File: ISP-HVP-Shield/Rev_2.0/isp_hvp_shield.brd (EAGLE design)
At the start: 50 x 53 mm, 26 parts, among them IC1 ATtiny13/15/25/45/85, IC2 ATtiny24/44/84, IC3 TINY26/261/461/861, IC4 ATtiny2313/4313, IC5 ATMEGA328, IC6 74HCT595D, IC7 MAX662A, Q1 BC858BSMD

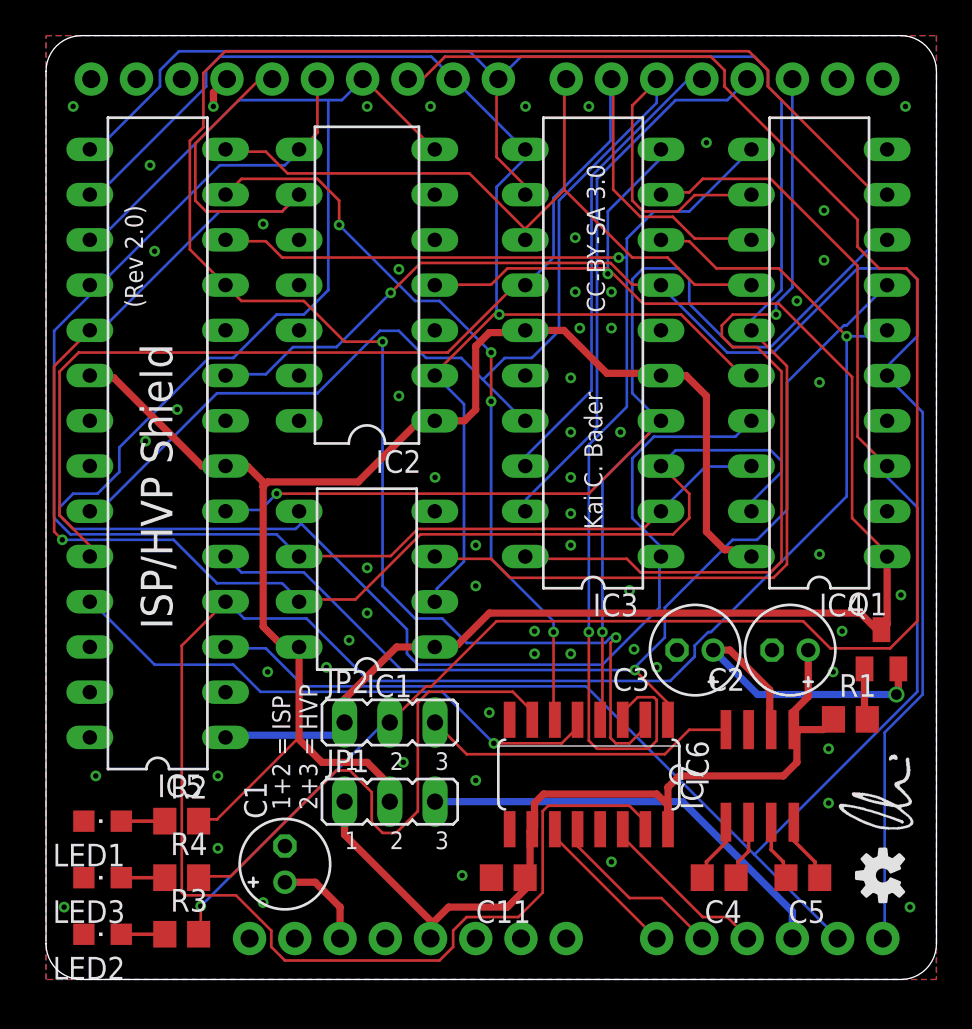
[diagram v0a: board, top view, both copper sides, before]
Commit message: New design. Started to add HVSP/HVPP features.
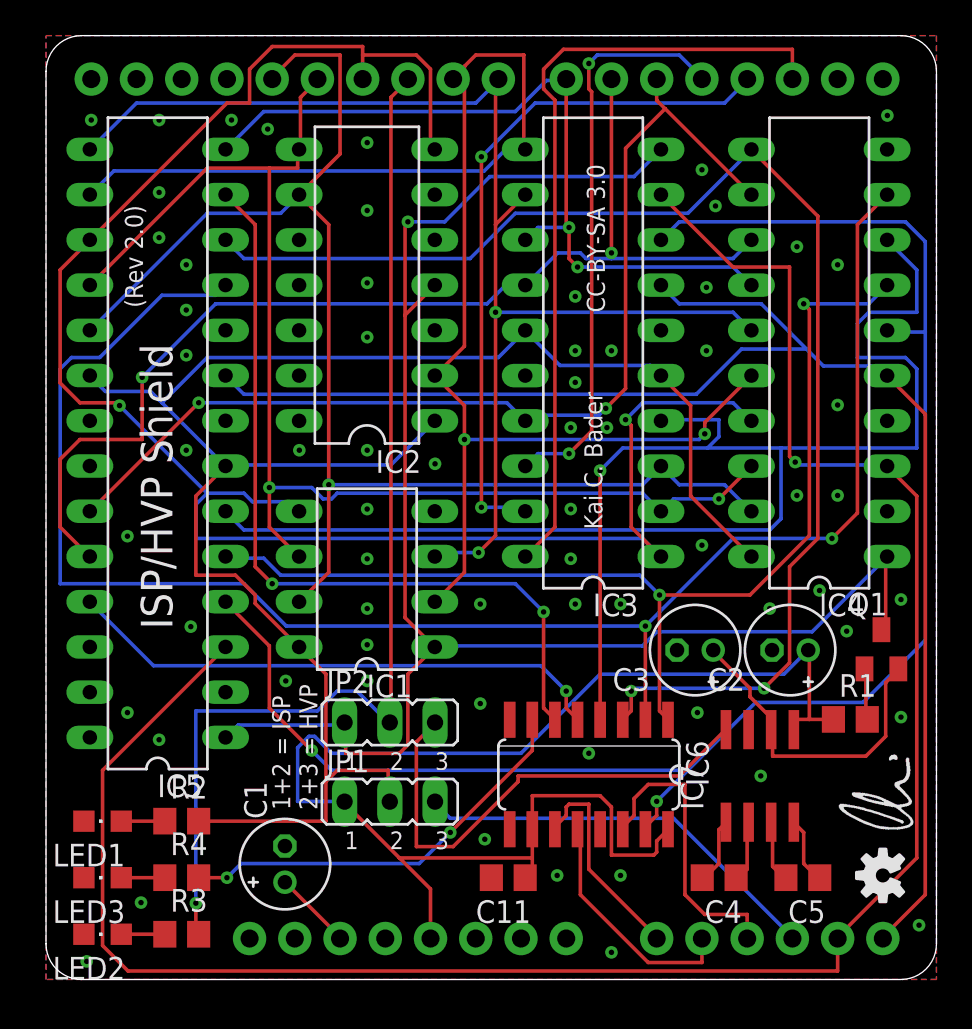
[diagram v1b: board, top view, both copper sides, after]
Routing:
- net D10: track 104.7 -> 61.3 mm
- net D8: track 99.7 -> 71.4 mm, vias 0 -> 2
- net VCC: track 49.9 -> 77.6 mm
- net Q0: track 118.5 -> 92.9 mm, vias 1 -> 2
- net A4: track 92.9 -> 117.6 mm, vias 0 -> 1
- net D13_SCK: track 96.4 -> 77.6 mm
- net Q4: track 73.1 -> 91.6 mm, vias 2 -> 1
- net +5V: track 85.5 -> 103.3 mm
- net D11_MOSI: track 113.8 -> 102.4 mm, vias 0 -> 2
- net D9: track 75.1 -> 85.5 mm, vias 1 -> 2
- net N$1: track 17.6 -> 27.7 mm
- net D5: track 67.2 -> 59.2 mm, vias 0 -> 2
- net Q7: track 31.4 -> 23.4 mm, vias 0 -> 2
- net D3: track 31.1 -> 39.0 mm, vias 0 -> 2
- net Q2: track 102.9 -> 95.5 mm
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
